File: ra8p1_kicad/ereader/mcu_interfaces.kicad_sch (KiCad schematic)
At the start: 1 part, among them U1 R7KA8P1KFLCAC#UC0

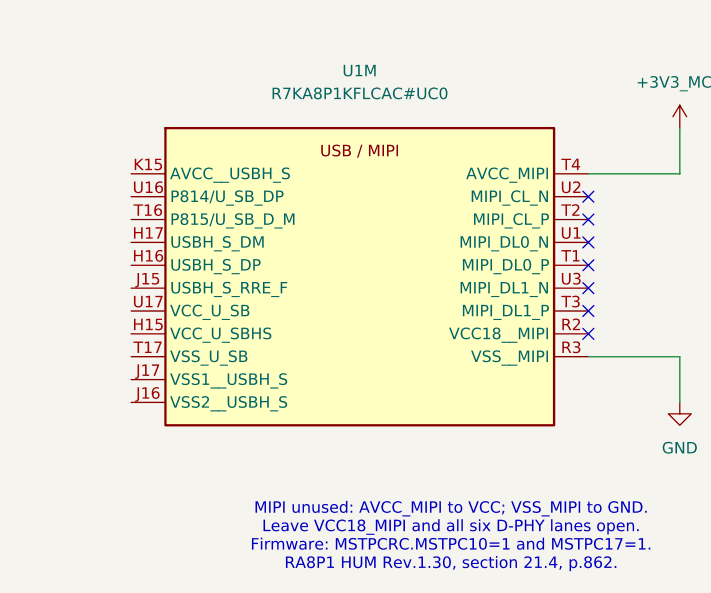
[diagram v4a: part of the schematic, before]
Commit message: feat(hardware): qualify USB supply pins and connect grounds
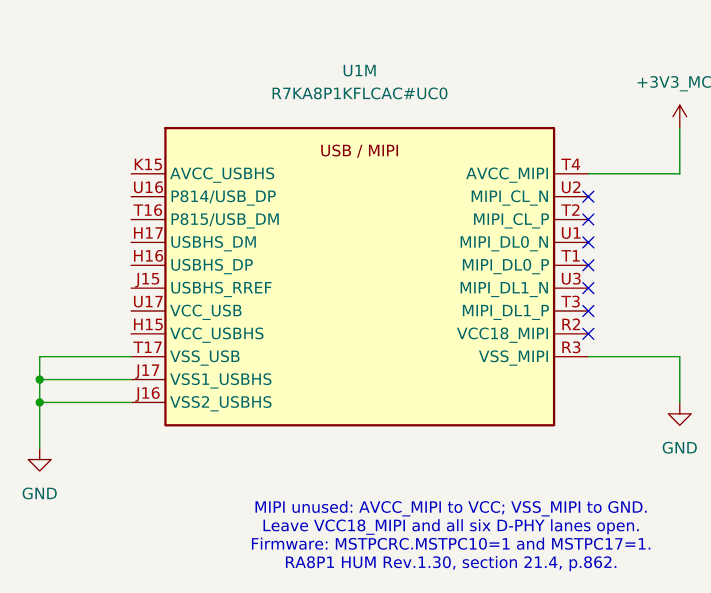
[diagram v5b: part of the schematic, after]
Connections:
- net GND: now also U1.J16 (VSS2_USBHS), U1.J17 (VSS1_USBHS), U1.T17 (VSS_USB)
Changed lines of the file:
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@@
 		)
 	)
+	(junction
+		(at 20.32 220.98)
+		(diameter 0)
+		(color 0 0 0 0)
+	)
+	(junction
+		(at 20.32 218.44)
+		(diameter 0)
+		(color 0 0 0 0)
+	)
 	(no_connect
 		(at 81.28 213.36)
@@
 	(wire
 		(pts
+			(xy 20.32 220.98) (xy 30.48 220.98)
+		)
+		(stroke
+			(width 0)
+			(type default)
+		)
+	)
+	(wire
+		(pts
+			(xy 20.32 215.9) (xy 30.48 215.9)
+		)
+		(stroke
+			(width 0)
+			(type default)
+		)
+	)
+	(wire
+		(pts
 			(xy 91.44 220.98) (xy 91.44 215.9)
 		)
@@
 	(wire
 		(pts
+			(xy 20.32 226.06) (xy 20.32 220.98)
+		)
+		(stroke
+			(width 0)
+			(type default)
+		)
+	)
+	(wire
+		(pts
+			(xy 20.32 218.44) (xy 30.48 218.44)
+		)
+		(stroke
+			(width 0)
+			(type default)
+		)
+	)
+	(wire
+		(pts
+			(xy 20.32 220.98) (xy 20.32 218.44)
+		)
+		(stroke
+			(width 0)
+			(type default)
+		)
+	)
+	(wire
+		(pts
 			(xy 81.28 195.58) (xy 91.44 195.58)
 		)
@@
 		)
 	)
+	(wire
+		(pts
+			(xy 20.32 218.44) (xy 20.32 215.9)
+		)
+		(stroke
+			(width 0)
+			(type default)
+		)
+	)
 	(symbol
 		(lib_id "Processors:R7KA8P1KFLCAC#UC0")
@@
 					(unit 1)
 				)
+			)
+		)
+	)
+	(symbol
+		(lib_id "power:GND")
+		(at 20.32 226.06 0)
+		(unit 1)
+		(body_style 1)
+		(exclude_from_sim no)
+		(in_bom yes)
+		(on_board yes)
+		(in_pos_files yes)
+		(dnp no)
+		(fields_autoplaced yes)
+		(property "Reference" "#PWR036"
+			(at 20.32 232.41 0)
+			(hide yes)
+			(show_name no)
+			(do_not_autoplace no)
+			(effects
+				(font
+					(size 1.27 1.27)
+				)
+			)
+		)
+		(property "Value" "GND"
+			(at 20.32 231.14 0)
+			(show_name no)
+			(do_not_autoplace no)
+			(effects
+				(font
+					(size 1.27 1.27)
+				)
+			)
+		)
+		(property "Footprint" ""
+			(at 20.32 226.06 0)
+			(hide yes)
+			(show_name no)
+			(do_not_autoplace no)
+			(effects
+				(font
+					(size 1.27 1.27)
+				)
+			)
+		)
+		(property "Datasheet" ""
+			(at 20.32 226.06 0)
+			(hide yes)
+			(show_name no)
+			(do_not_autoplace no)
+			(effects
+				(font
+					(size 1.27 1.27)
+				)
+			)
+		)
+		(property "Description" "Power symbol creates a global label with name \"GND\" , ground"
+			(at 20.32 226.06 0)
+			(hide yes)
+			(show_name no)
+			(do_not_autoplace no)
+			(effects
+				(font
+					(size 1.27 1.27)
+				)
+			)
+		)
+		(pin "1"
+		)
+		(instances
+			(project "ereader_rev1"
+				(path "/0586cc51-9c57-495b-a0c9-c29ba0d48166/33c39500-46ef-4bfe-91bb-bf0f803ca6e5"
+					(reference "#PWR036")
+					(unit 1)
+				)

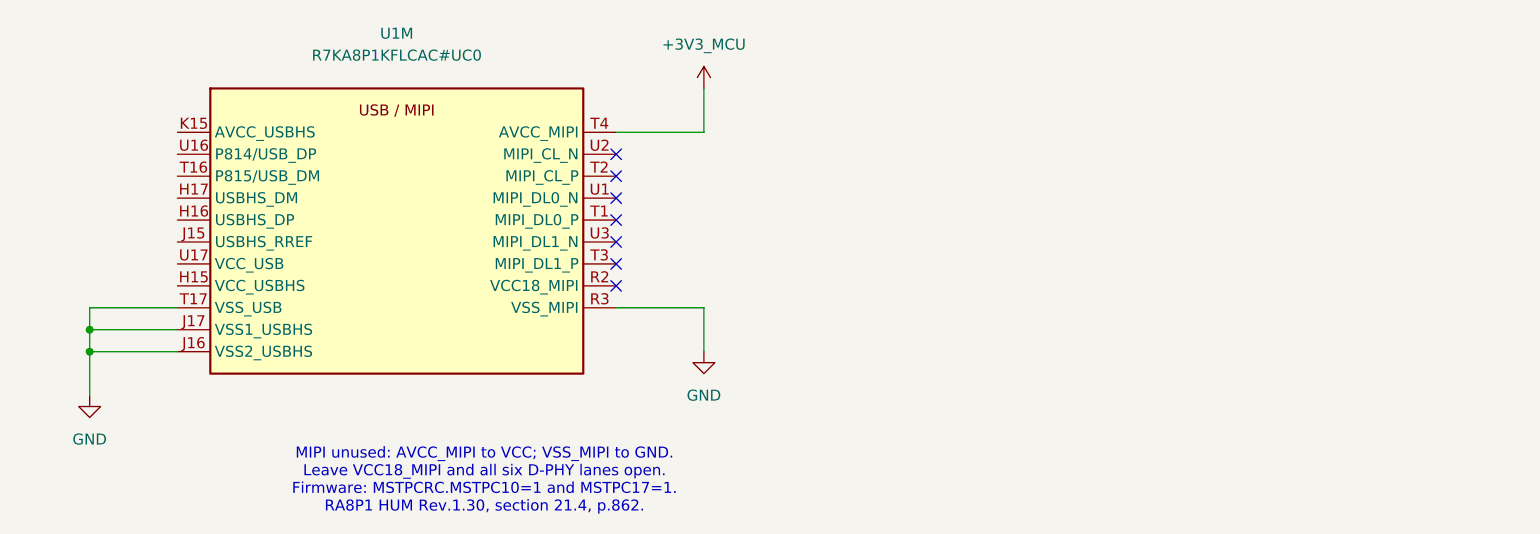
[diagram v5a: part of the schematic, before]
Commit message: feat(hardware): add sourced USBHS reference resistor
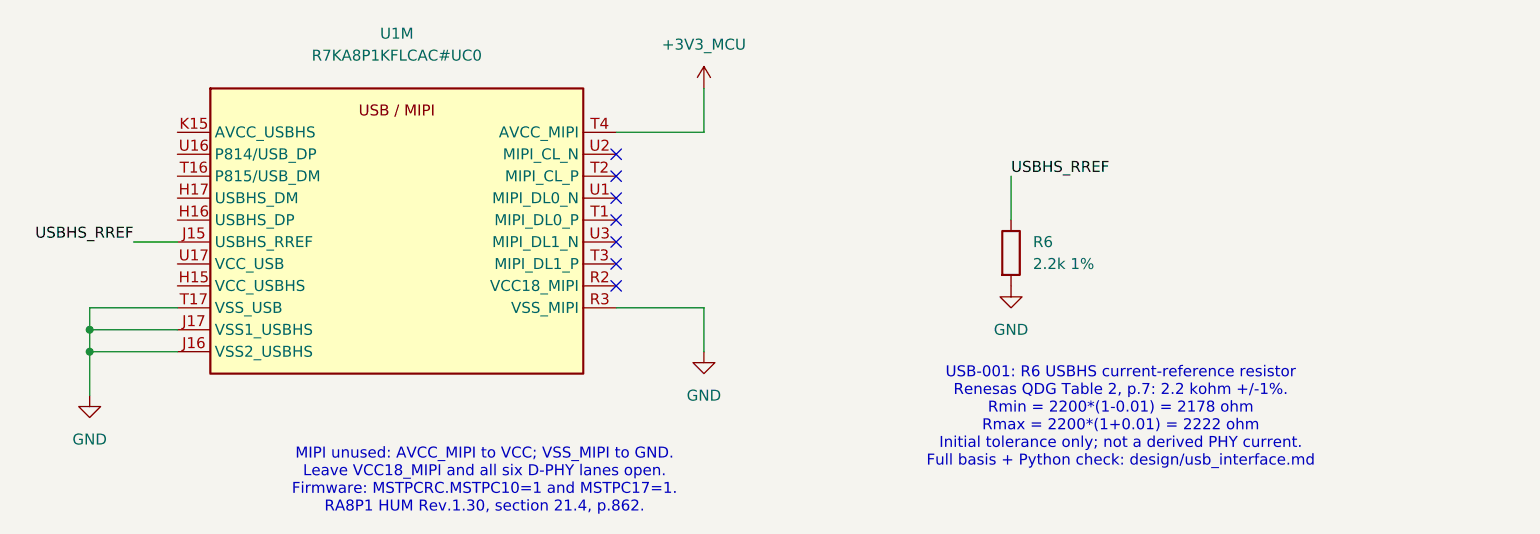
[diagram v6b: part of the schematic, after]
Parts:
- added R6: 2.2k 1%, symbol Device:R
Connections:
- net GND: now also R6.2
- net USBHS_RREF: now reaches U1.J15 (USBHS_RREF)
- net USBHS_RREF: now also R6.1
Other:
- note added: "USB-001: R6 USBHS current-reference resistor Renesas QDG Table 2, p.7: 2.2 kohm +/-1%. Rmin = 2200*(1-0.01) = 2178 ohm Rmax = 2200*(1+0.01) = 2222 ohm Initial tolerance only; not a derived PHY current. Full basis + Python check: design/usb_interface.md"

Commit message: feat(hardware): add MIPI analog supply bypass
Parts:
- added C39: 100n, symbol Device:C_Small
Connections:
- net +3V3_MCU: now also C39.1
- net GND: now also C39.2
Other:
- note added: "PWR-001: C39 AVCC_MIPI bypass, 100 nF (QDG Table 2, p.7). TDK C1608X7R1H104K080AA; 50 V X7R, +/-10%. Initial C = 100*(1 +/-0.10) = 90..110 nF. Voltage utilization: 3.3/50*100 = 6.6%; at 3.6 V: 7.2%. DC bias, aging and final rail qualification remain open. Full basis + Python check: design/power_decoupling.md"

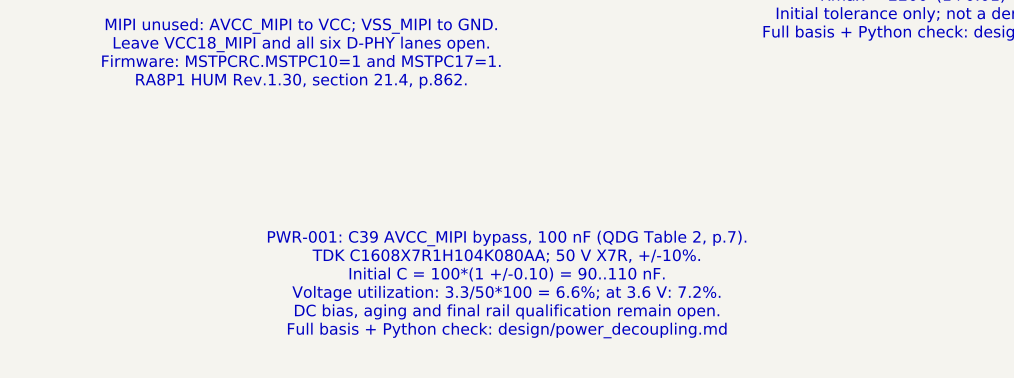
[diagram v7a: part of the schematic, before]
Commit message: feat(hardware): source and screen MCU bypass capacitors
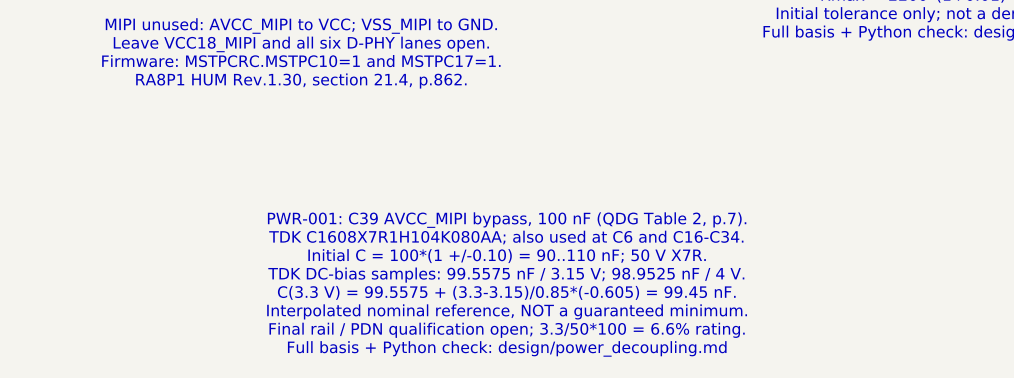
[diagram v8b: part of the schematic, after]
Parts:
- C39: Procurement_Status Candidate - nominal ratings sourced; DC bias qualification 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 -> Selected - nominal DC-bias screened; final rail and PDN qua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; Selection_Basis Renesas QDG Table 2: AVCC_MIPI bypass 100 nF. 100 nF +/-10%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 -> Renesas QDG Table 2: AVCC_MIPI 100 nF bypass. 50 V X7R +/-1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; Sourcing_Snapshot 2026-09-05: DigiKey Active, 374087 in stock, 24 weeks; USD 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 -> 2026-09-05: TDK Production; DigiKey Active, 374087 in stock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
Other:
- note added: "PWR-001: C39 AVCC_MIPI bypass, 100 nF (QDG Table 2, p.7). TDK C1608X7R1H104K080AA; also used at C6 and C16-C34. Initial C = 100*(1 +/-0.10) = 90..110 nF; 50 V X7R. TDK DC-bias samples: 99.5575 nF / 3.15 V; 98.9525 nF / 4 V. C(3.3 V) = 99.5575 + (3.3-3.15)/0.85*(-0.605) = 99.45 nF. Interpolated nominal reference, NOT a guaranteed minimum. Final rail / PDN qualification open; 3.3/50*100 = 6.6% rati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"
- note removed: "PWR-001: C39 AVCC_MIPI bypass, 100 nF (QDG Table 2, p.7). TDK C1608X7R1H104K080AA; 50 V X7R, +/-10%. Initial C = 100*(1 +/-0.10) = 90..110 nF. Voltage utilization: 3.3/50*100 = 6.6%; at 3.6 V: 7.2%. DC bias, aging and final rail qualification remain open. Full basis + Python check: design/power_decoupling.md"
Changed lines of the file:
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@@
 		)
 	)
-	(text "PWR-001: C39 AVCC_MIPI bypass, 100 nF (QDG Table 2, p.7).\nTDK C1608X7R1H104K080AA; 50 V X7R, +/-10%.\nInitial C = 100*(1 +/-0.10) = 90..110 nF.\nVoltage utilization: 3.3/50*100 = 6.6%; at 3.6 V: 7.2%.\nDC bias, aging and final rail qualification remain open.\nFull basis + Python check: design/power_decoupling.md"
+	(text "PWR-001: C39 AVCC_MIPI bypass, 100 nF (QDG Table 2, p.7).\nTDK C1608X7R1H104K080AA; also used at C6 and C16-C34.\nInitial C = 100*(1 +/-0.10) = 90..110 nF; 50 V X7R.\nTDK DC-bias samples: 99.5575 nF / 3.15 V; 98.9525 nF / 4 V.\nC(3.3 V) = 99.5575 + (3.3-3.15)/0.85*(-0.605) = 99.45 nF.\nInterpolated nominal reference, NOT a guaranteed minimum.\nFinal rail / PDN qualification open; 3.3/50*100 = 6.6% rating.\nFull basis + Python check: design/power_decoupling.md"
 		(exclude_from_sim no)
 		(at 88.9 261.62 0)
@@
 			)
 		)
-		(property "Description" "TDK C1608X7R1H104K080AA; 100 nF +/-10%, 50 V X7R. MIPI AVCC bypass per Renesas QDG Table 2. DC bias qualification pending."
+		(property "Description" "TDK C1608X7R1H104K080AA; 100 nF +/-10%, 50 V X7R. MIPI AVCC bypass per Renesas QDG Table 2. Nominal DC-bias screened; final rail and PDN qualification open."
 			(at 101.6 203.2 0)
 			(hide yes)
@@
 			)
 		)
-		(property "Procurement_Status" "Candidate - nominal ratings sourced; DC bias qualification pending"
+		(property "Procurement_Status" "Selected - nominal DC-bias screened; final rail and PDN qualification open"
 			(at 101.6 203.2 0)
 			(hide yes)
@@
 			)
 		)
-		(property "Selection_Basis" "Renesas QDG Table 2: AVCC_MIPI bypass 100 nF. 100 nF +/-10%, 50 V X7R, -55 to 125 C. Effective capacitance/DC bias qualification pending."
+		(property "Selection_Basis" "Renesas QDG Table 2: AVCC_MIPI 100 nF bypass. 50 V X7R +/-10%; TDK nominal DC-bias curve: 99.45 nF at 3.3 V (interpolated reference, not guaranteed minimum). PWR-001 design/power_decoupling.md."
 			(at 101.6 203.2 0)
 			(hide yes)
@@
 			)
 		)
-		(property "Sourcing_Snapshot" "2026-09-05: DigiKey Active, 374087 in stock, 24 weeks; USD 1:0.11, 10:0.06, 100:0.0359."
+		(property "Sourcing_Snapshot" "2026-09-05: TDK Production; DigiKey Active, 374087 in stock, 24 weeks; USD 1:0.11, 10:0.06, 100:0.0359."
 			(at 101.6 203.2 0)
 			(hide yes)
